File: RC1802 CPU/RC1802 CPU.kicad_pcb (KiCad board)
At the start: 2 copper layers, 99.1 x 99.1 mm, 49 parts, among them J1 Mount, J2 Mount, J3 Mount, J4 Mount, J5 CONN_01X39, J6 CONN_02X20, J7 BARREL_JACK, J9 Conn_Q, U1 74LS04, U2 CDP1802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

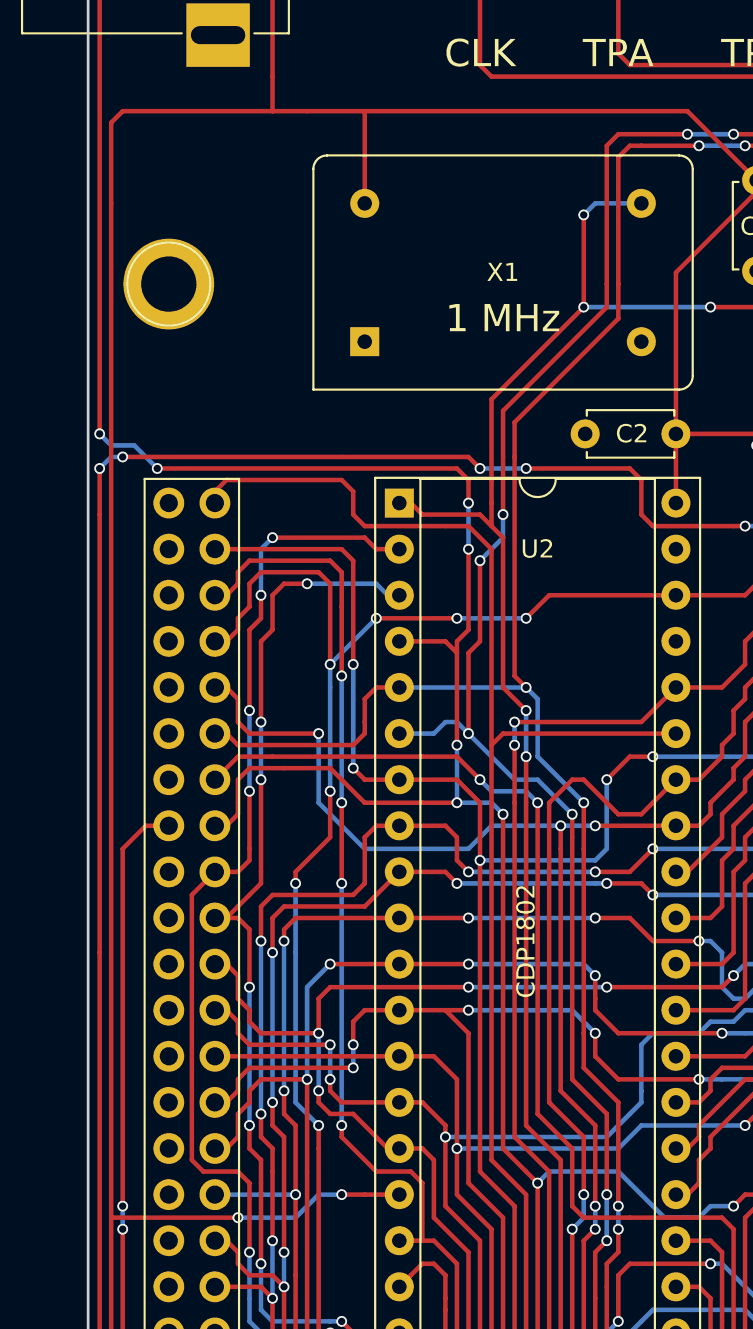
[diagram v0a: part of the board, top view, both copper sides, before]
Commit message: Gerber export CPU board after adding clockport
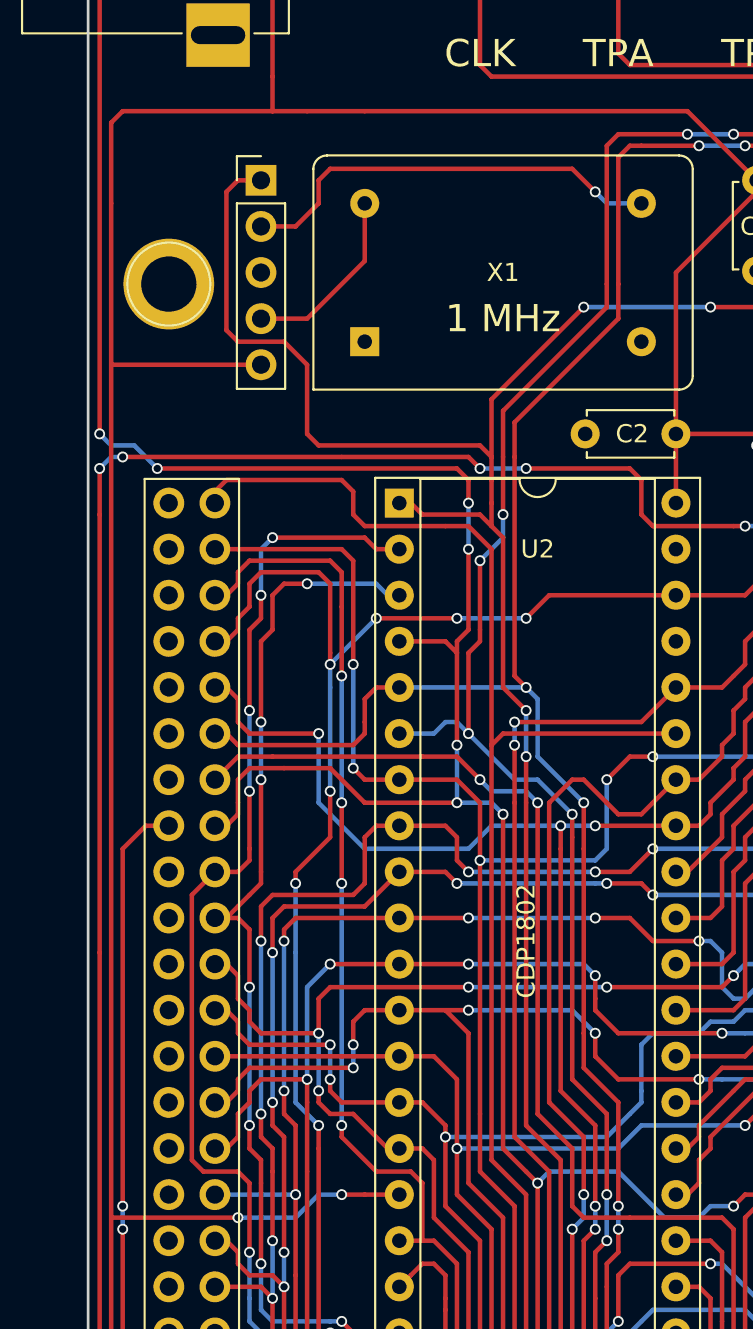
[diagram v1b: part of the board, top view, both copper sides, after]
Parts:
- added J8: ClockPort, Pin_Headers:Pin_Header_Straight_1x05_Pitch2.54mm, F.Cu at (109.9, 66.0)
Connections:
- X1 pad 14: VCC -> /CLK_PWR
- X1 pad 8: CLOCK -> Net-(J8-Pad2)
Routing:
- net Net-(J8-Pad2): track 0.00 -> 23.8 mm, vias 0 -> 1
- net CLOCK: track 127.1 -> 148.1 mm, vias 8 -> 7
- net /CLK_PWR: track 0.00 -> 10.2 mm
- net VCC: track 433.0 -> 436.2 mm

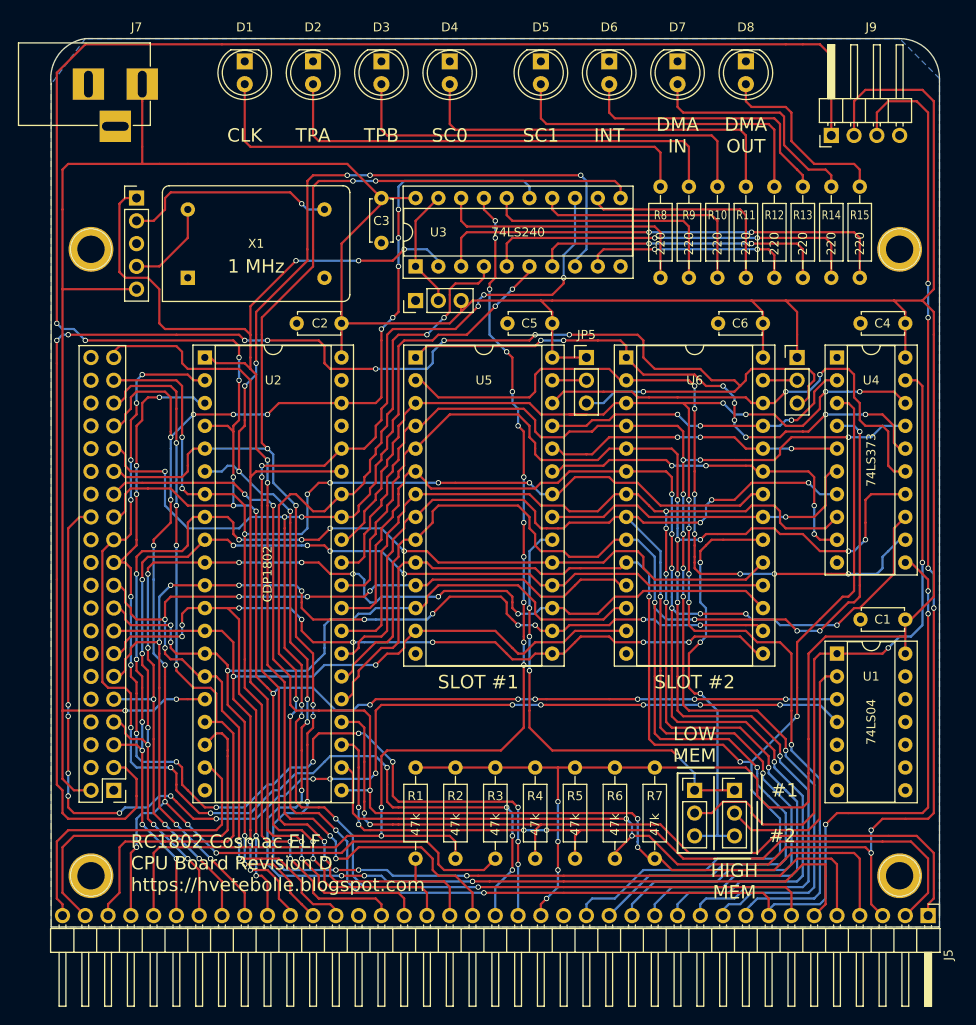
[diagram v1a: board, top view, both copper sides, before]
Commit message: Added jumpers for inverting TX/RX
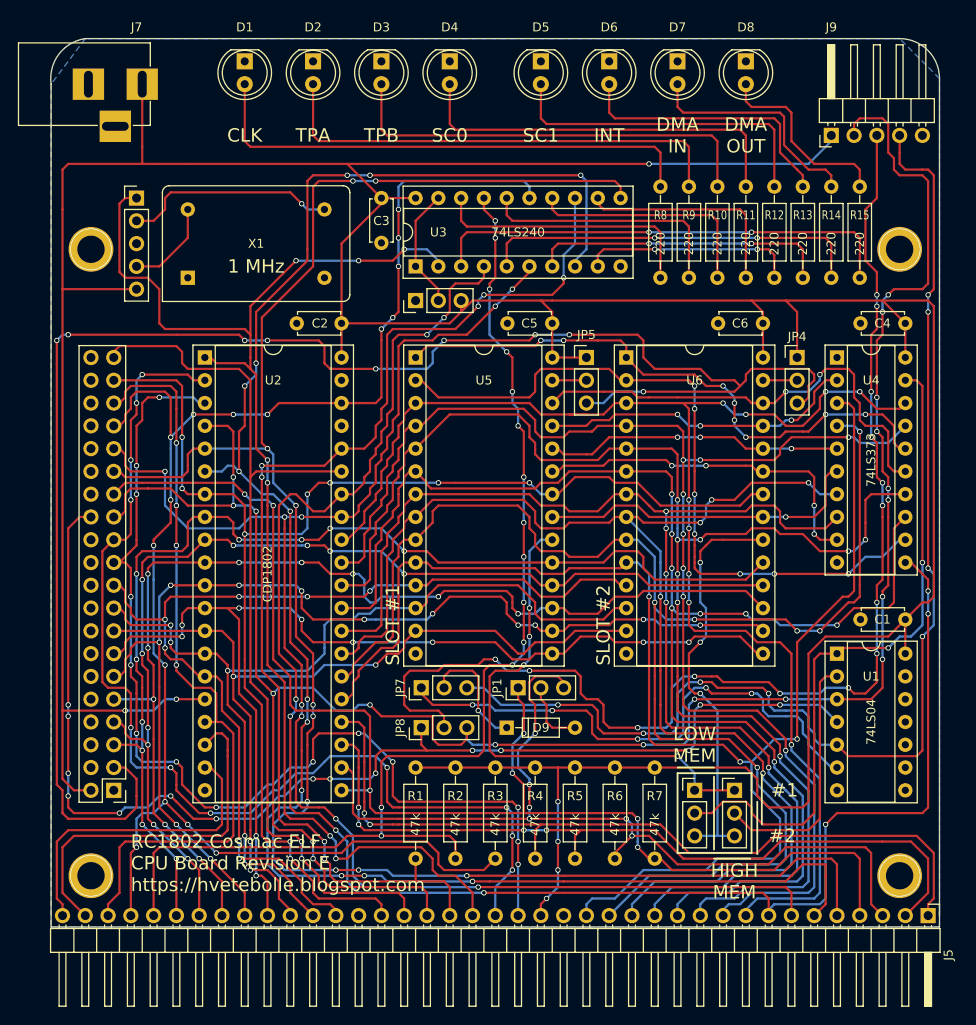
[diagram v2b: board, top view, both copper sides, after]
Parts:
- added D9: 1N4148, Diodes_THT:D_DO-35_SOD27_P7.62mm_Horizontal, F.Cu at (151.1, 125.1)
- added JP1: RX_SEL, Pin_Headers:Pin_Header_Straight_1x03_Pitch2.54mm, F.Cu at (152.4, 120.7)
- added JP7: RX_INVERT, Pin_Headers:Pin_Header_Straight_1x03_Pitch2.54mm, F.Cu at (141.6, 120.7)
- added JP8: TX_INVERT, Pin_Headers:Pin_Header_Straight_1x03_Pitch2.54mm, F.Cu at (141.6, 125.1)
- J5: value CONN_01X39 -> Expansion
- J6: value CONN_02X20 -> UI_Connector
- J9: value Conn_Q -> Q_Connector; footprint Pin_Headers:Pin_Header_Angled_1x04_Pitch2.54mm -> Pin_Headers:Pin_Header_Angled_1x05_Pitch2.54mm
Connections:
- net /~Q renamed ~Q
- J9 pad 1: Q -> VCC
- J9 pad 2: VCC -> Q
- J9 pad 3: EF3 -> TX
- J9 pad 4: GND -> RX
- U1 pad 5: GND -> RX
- U1 pad 6: (no net) -> Net-(JP7-Pad1)
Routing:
- net TX: track 0.00 -> 137.8 mm, vias 0 -> 14
- net RX: track 0.00 -> 136.9 mm, vias 0 -> 8
- net EF3: track 176.8 -> 100.6 mm, vias 8 -> 6
- net Q: track 312.4 -> 249.1 mm, vias 16 -> 19
- net Net-(JP7-Pad1): track 0.00 -> 60.4 mm, vias 0 -> 5
- net VCC: track 436.2 -> 457.1 mm, vias 6 -> 7
- net EF4: track 132.5 -> 147.8 mm, vias 5 -> 7
- net Net-(D9-Pad1): track 0.00 -> 13.4 mm, vias 0 -> 1
- net SLOT1_CS: track 49.6 -> 58.9 mm
- net Net-(D9-Pad2): track 0.00 -> 8.15 mm
- net ~Q: track 132.2 -> 134.2 mm
- net /MA4: track 157.7 -> 159.6 mm
- net /MA0: track 162.4 -> 163.9 mm
- net /MA12: track 81.5 -> 80.8 mm
- net /MA6: track 153.5 -> 154.0 mm
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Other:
- board text added: "RC1802 Cosmac ELF CPU Board Revision E https://hvetebolle.blogspot.com"
- board text added: "RX"
- board text added: "TX"
- board text removed: "EF3"
- board text removed: "RC1802 Cosmac ELF CPU Board Revision D https://hvetebolle.blogspot.com"

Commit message: Wider power tracks and moved clockport
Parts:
- moved J8 5.85 mm to (114.3, 62.2), turned to 90 degrees
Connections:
- J6 pad 40: GND -> VCC
- J6 pad 8: GND -> (no net)
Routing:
- net VCC: track 457.1 -> 449.7 mm
- net Net-(J8-Pad2): track 23.8 -> 25.9 mm
- net CLOCK: track 148.1 -> 146.9 mm
- net Net-(D1-Pad2): track 57.0 -> 55.9 mm
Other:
- net class VCC added: clearance 0.2, trace_width 0.75, via_dia 0.6, via_drill 0.4

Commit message: Added clock in and out to UI connector
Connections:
- J6 pad 32: (no net) -> CLOCK_OUT
- J6 pad 34: (no net) -> CLOCK
- J8 pad 2: Net-(J8-Pad2) -> CLOCK_OUT
- X1 pad 8: Net-(J8-Pad2) -> CLOCK_OUT
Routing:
- net CLOCK_OUT: track 0.00 -> 57.4 mm, vias 0 -> 3
- net Net-(J8-Pad2): track 25.9 -> 0.00 mm, vias 1 -> 0
- net CLOCK: track 146.9 -> 165.4 mm, vias 7 -> 8
- net MWR: track 102.6 -> 99.8 mm
- net VCC: track 449.7 -> 451.7 mm

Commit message: Fixed DMA_OUT fault in schematic and layout
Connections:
- U2 pad 37: (no net) -> DMA_OUT
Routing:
- net DMA_OUT: track 131.1 -> 151.5 mm, vias 14 -> 16
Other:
- board text added: "RC1802 Cosmac ELF CPU Board Revision F github.com/tebl"
- board text removed: "RC1802 Cosmac ELF CPU Board Revision E https://hvetebolle.blogspot.com"

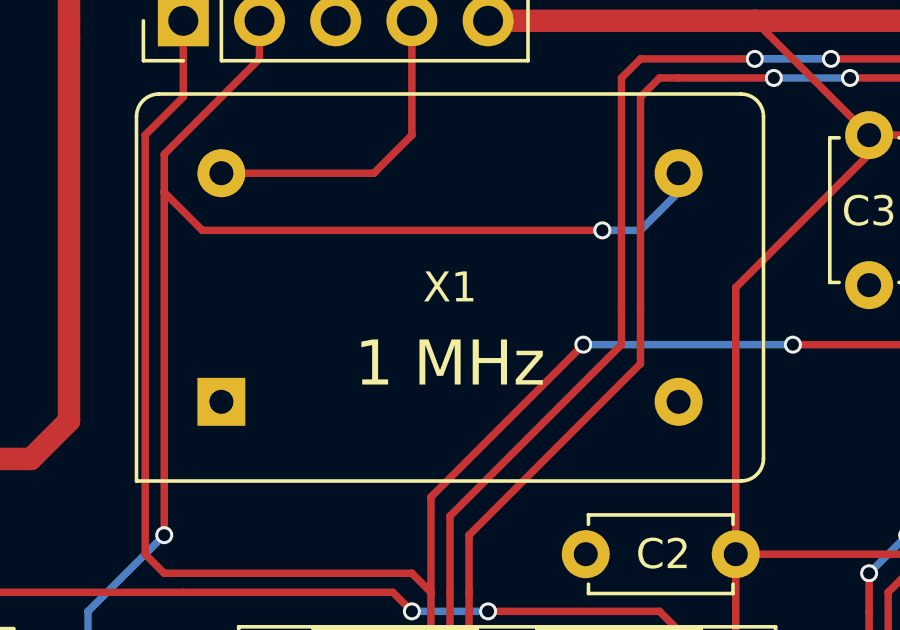
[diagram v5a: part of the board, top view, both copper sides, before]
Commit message: KiCad 5 update, both boards now marked F to match (without any actual changes)
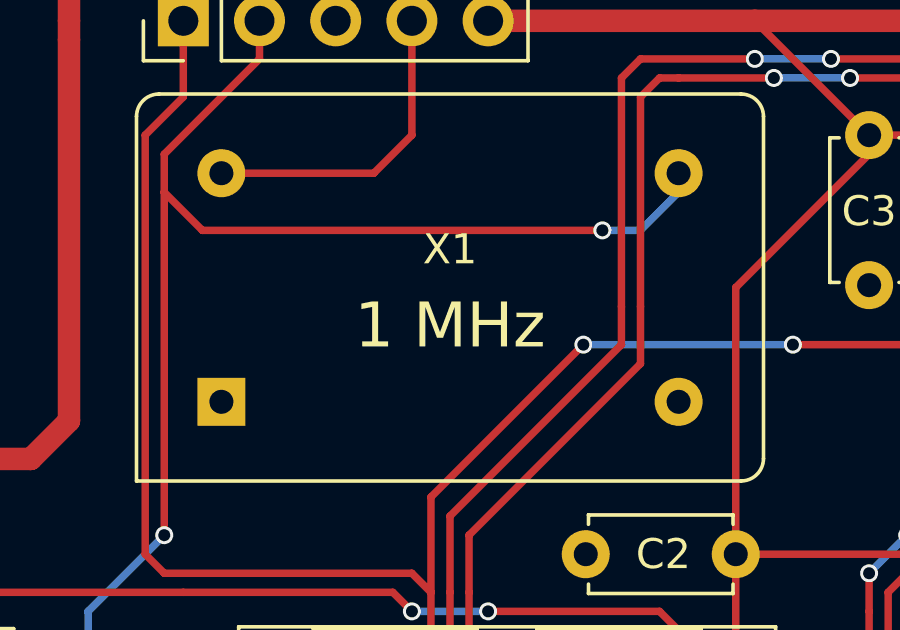
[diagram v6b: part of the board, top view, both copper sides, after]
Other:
- board text added: "OSC OUT"
- board text added: "OSC PWR"
